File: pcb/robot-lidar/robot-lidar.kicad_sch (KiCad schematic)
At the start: 29 parts, among them J2 YLIDAR X4, J3 Jack-DC, J5 Conn_02x03_Odd_Even, J7 Conn_ARM_SWD_TagConnect_TC2030, U1 STM32F429VETx, U2 LM317-3.3_SOT-223, U2 MPU-6050, Y1 Crystal

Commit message: add rst
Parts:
- added R4: 10k, Resistor_SMD:R_0603_1608Metric, symbol Device:R_Small
- added SW1: SW_SPST, Button_Switch_SMD:SW_SPST_CK_RS282G05A3, symbol Switch:SW_SPST
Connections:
- net +3V3: now also R4.2
- net GND: now also SW1.1 (A)
- net RESET: now also U1.14 (NRST), R4.1, SW1.2 (B)
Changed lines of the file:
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@@
   (junction (at 237.49 97.79) (diameter 0) (color 0 0 0 0)
   )
+  (junction (at 52.07 49.53) (diameter 0) (color 0 0 0 0)
+  )
   (junction (at 85.09 21.59) (diameter 0) (color 0 0 0 0)
   )
@@
   (junction (at 242.57 59.69) (diameter 0) (color 0 0 0 0)
   )
+  (junction (at 48.26 49.53) (diameter 0) (color 0 0 0 0)
+  )
   (junction (at 236.22 -19.05) (diameter 0) (color 0 0 0 0)
   )
@@
     (stroke (width 0) (type default))
   )
+  (wire (pts (xy 52.07 49.53) (xy 54.61 49.53))
+    (stroke (width 0) (type default))
+  )
   (wire (pts (xy 87.63 21.59) (xy 87.63 41.91))
     (stroke (width 0) (type default))
   )
+  (wire (pts (xy 31.75 49.53) (xy 34.29 49.53))
+    (stroke (width 0) (type default))
+  )
   (wire (pts (xy 232.41 97.79) (xy 237.49 97.79))
     (stroke (width 0) (type default))
@@
     (stroke (width 0) (type default))
   )
+  (wire (pts (xy 48.26 49.53) (xy 52.07 49.53))
+    (stroke (width 0) (type default))
+  )
   (wire (pts (xy 229.87 -19.05) (xy 236.22 -19.05))
     (stroke (width 0) (type default))
@@
     (stroke (width 0) (type default))
   )
+  (wire (pts (xy 48.26 40.64) (xy 48.26 43.18))
+    (stroke (width 0) (type default))
+  )
   (wire (pts (xy 208.28 123.19) (xy 208.28 135.89))
     (stroke (width 0) (type default))
@@
     (stroke (width 0) (type default))
   )
+  (wire (pts (xy 48.26 49.53) (xy 48.26 48.26))
+    (stroke (width 0) (type default))
+  )
   (wire (pts (xy 261.62 59.69) (xy 270.51 59.69))
     (stroke (width 0) (type default))
@@
     (stroke (width 0) (type default))
   )
+  (wire (pts (xy 31.75 49.53) (xy 31.75 50.8))
+    (stroke (width 0) (type default))
+  )
   (wire (pts (xy 237.49 97.79) (xy 241.3 97.79))
     (stroke (width 0) (type default))
@@
     (stroke (width 0) (type default))
   )
+  (wire (pts (xy 44.45 49.53) (xy 48.26 49.53))
+    (stroke (width 0) (type default))
+  )
   (wire (pts (xy 77.47 184.15) (xy 77.47 190.5))
     (stroke (width 0) (type default))
@@
   )
   (wire (pts (xy 261.62 71.12) (xy 261.62 69.85))
+    (stroke (width 0) (type default))
+  )
+  (wire (pts (xy 52.07 48.26) (xy 52.07 49.53))
     (stroke (width 0) (type default))
   )
@@
     )
   )
+  (global_label "RESET" (shape input) (at 52.07 48.26 90) (fields_autoplaced)
+    (effects (font (size 1.27 1.27)) (justify left))
+    (property "Intersheetrefs" "${INTERSHEET_REFS}" (at 52.07 39.5297 90)
+      (effects (font (size 1.27 1.27)) (justify left) hide)
+    )
+  )
   (symbol (lib_id "Device:R_Small") (at 171.45 -16.51 270) (unit 1)
     (in_bom yes) (on_board yes) (dnp no)
@@
     )
   )
+  (symbol (lib_id "Switch:SW_SPST") (at 39.37 49.53 0) (unit 1)
+    (in_bom yes) (on_board yes) (dnp no) (fields_autoplaced)
+    (property "Reference" "SW1" (at 39.37 43.18 0)
+      (effects (font (size 1.27 1.27)))
+    )
+    (property "Value" "SW_SPST" (at 39.37 45.72 0)
+      (effects (font (size 1.27 1.27)))
+    )
+    (property "Footprint" "Button_Switch_SMD:SW_SPST_CK_RS282G05A3" (at 39.37 49.53 0)
+      (effects (font (size 1.27 1.27)) hide)
+    )
+    (property "Datasheet" "~" (at 39.37 49.53 0)
+      (effects (font (size 1.27 1.27)) hide)
+    )
+    (pin "1")
+    (pin "2")
+    (instances
+      (project "tablet"
+        (path "/868516f5-1ea3-47ae-b277-3f67998564bb"
+          (reference "SW1") (unit 1)
+        )
+      )
+      (project "robot-lidar"
+        (path "/cb10bbf7-c2c1-4a0d-8947-ad707931d83b"
+          (reference "SW1") (unit 1)
+        )
+      )
+    )
+  )
   (symbol (lib_id "Device:C") (at 270.51 128.27 0) (unit 1)
     (in_bom yes) (on_board yes) (dnp no) (fields_autoplaced)
@@
         (path "/cb10bbf7-c2c1-4a0d-8947-ad707931d83b"
           (reference "#PWR05") (unit 1)
+        )
+      )
+    )
+  )
+  (symbol (lib_id "Device:R_Small") (at 48.26 45.72 180) (unit 1)
+    (in_bom yes) (on_board yes) (dnp no)
+    (property "Reference" "R4" (at 44.45 41.91 90)
+      (effects (font (size 1.27 1.27)))
+    )
+    (property "Value" "10k" (at 46.99 41.91 90)
+      (effects (font (size 1.27 1.27)))
+    )
+    (property "Footprint" "Resistor_SMD:R_0603_1608Metric" (at 48.26 45.72 0)
+      (effects (font (size 1.27 1.27)) hide)
+    )
+    (property "Datasheet" "~" (at 48.26 45.72 0)
+      (effects (font (size 1.27 1.27)) hide)
+    )
+    (pin "1")
+    (pin "2")
+    (instances
+      (project "tablet"
+        (path "/868516f5-1ea3-47ae-b277-3f67998564bb"
+          (reference "R4") (unit 1)
+        )
+      )
+      (project "robot-lidar"
+        (path "/cb10bbf7-c2c1-4a0d-8947-ad707931d83b"
+          (reference "R7") (unit 1)
         )
       )
@@
     )
   )
+  (symbol (lib_id "power:+3V3") (at 48.26 40.64 0) (unit 1)
+    (in_bom yes) (on_board yes) (dnp no)
+    (property "Reference" "#PWR012" (at 48.26 44.45 0)
+      (effects (font (size 1.27 1.27)) hide)
+    )
+    (property "Value" "+3V3" (at 44.45 38.1 0)
+      (effects (font (size 1.27 1.27)))
+    )
+    (property "Footprint" "" (at 48.26 40.64 0)
+      (effects (font (size 1.27 1.27)) hide)
+    )
+    (property "Datasheet" "" (at 48.26 40.64 0)
+      (effects (font (size 1.27 1.27)) hide)
+    )
+    (pin "1")
+    (instances
+      (project "tablet"
+        (path "/868516f5-1ea3-47ae-b277-3f67998564bb"
+          (reference "#PWR012") (unit 1)
+        )
+      )
+      (project "robot-lidar"
+        (path "/cb10bbf7-c2c1-4a0d-8947-ad707931d83b"
+          (reference "#PWR021") (unit 1)
+        )
+      )
+    )
+  )
   (symbol (lib_id "power:+3V3") (at 115.57 -29.21 0) (unit 1)
     (in_bom yes) (on_board yes) (dnp no)
@@
         )
       )
+    )
+  )
+  (symbol (lib_id "power:GND") (at 31.75 50.8 0) (unit 1)
+    (in_bom yes) (on_board yes) (dnp no) (fields_autoplaced)
+    (property "Reference" "#PWR013" (at 31.75 57.15 0)
+      (effects (font (size 1.27 1.27)) hide)
+    )
+    (property "Value" "GND" (at 31.75 55.88 0)
+      (effects (font (size 1.27 1.27)))
+    )
+    (property "Footprint" "" (at 31.75 50.8 0)
+      (effects (font (size 1.27 1.27)) hide)
+    )
+    (property "Datasheet" "" (at 31.75 50.8 0)
+      (effects (font (size 1.27 1.27)) hide)
+    )
+    (pin "1")
+    (instances
+      (project "tablet"
+        (path "/868516f5-1ea3-47ae-b277-3f67998564bb"
+          (reference "#PWR013") (unit 1)
+        )
+      )
+      (project "robot-lidar"
+        (path "/cb10bbf7-c2c1-4a0d-8947-ad707931d83b"
+          (reference "#PWR020") (unit 1)
+        )
+      )

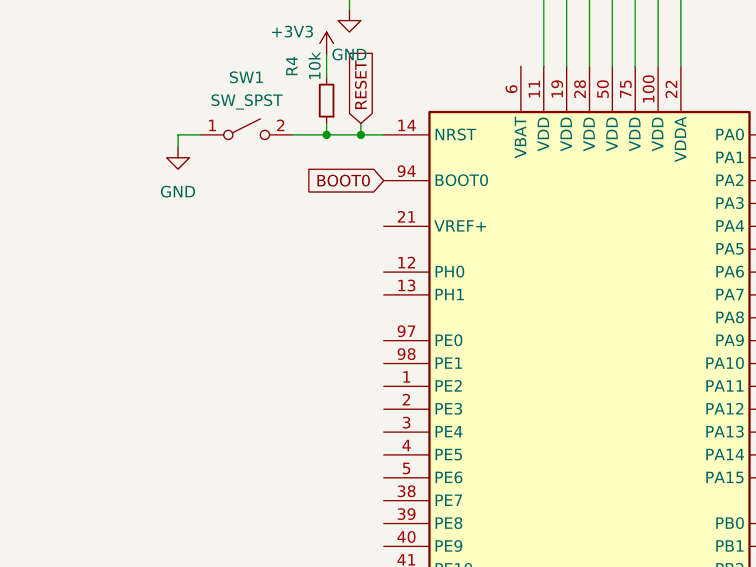
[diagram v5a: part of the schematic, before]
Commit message: wire crystal
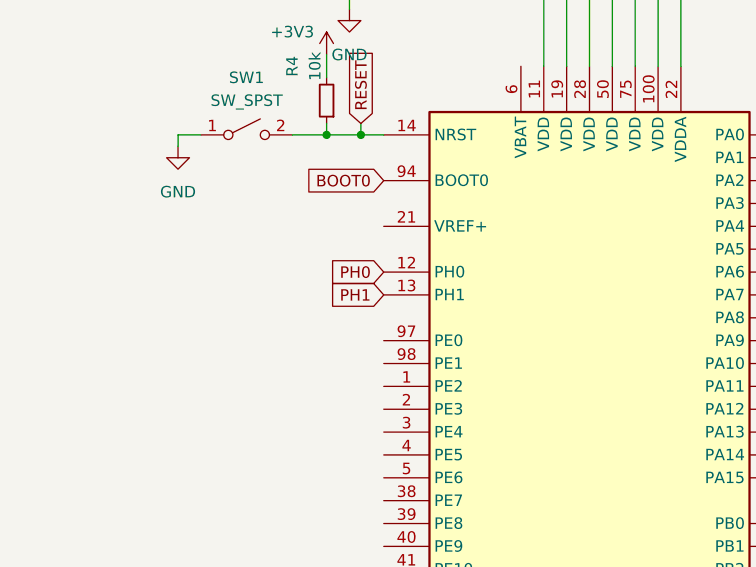
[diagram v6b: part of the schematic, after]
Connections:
- net PH0: now also U1.12 (PH0)
- net PH1: now also U1.13 (PH1)
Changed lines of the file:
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@@
+    )
+  )
+  (global_label "PH1" (shape input) (at 54.61 67.31 180) (fields_autoplaced)
+    (effects (font (size 1.27 1.27)) (justify right))
+    (property "Intersheetrefs" "${INTERSHEET_REFS}" (at 47.8148 67.31 0)
+      (effects (font (size 1.27 1.27)) (justify right) hide)
     )
   )
@@
     )
   )
+  (global_label "PH0" (shape input) (at 54.61 64.77 180) (fields_autoplaced)
+    (effects (font (size 1.27 1.27)) (justify right))
+    (property "Intersheetrefs" "${INTERSHEET_REFS}" (at 47.8148 64.77 0)
+      (effects (font (size 1.27 1.27)) (justify right) hide)
+    )
+  )

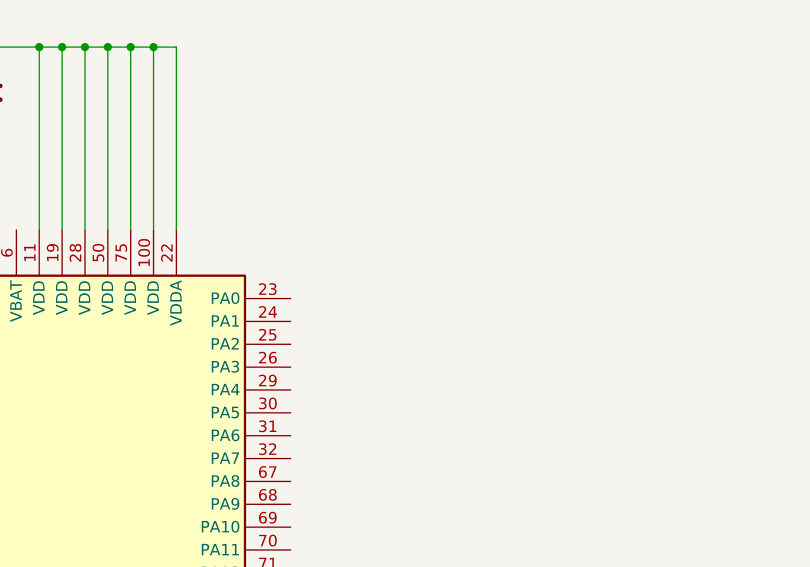
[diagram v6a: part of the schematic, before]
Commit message: add leds
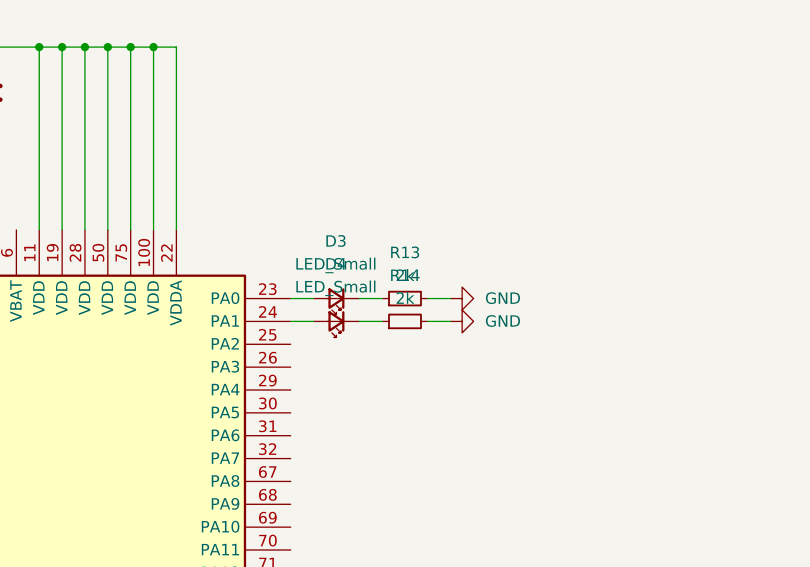
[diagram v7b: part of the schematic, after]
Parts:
- added D3, D4: LED_Small, Resistor_SMD:R_0603_1608Metric, symbol Device:LED_Small
- added R13, R14: 2k, Resistor_SMD:R_0603_1608Metric, symbol Device:R_Small
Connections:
- net GND: now also R13.2, R14.2
- net at U1.23 (PA0): now also D3.2 (A)
- net at U1.24 (PA1): now also D4.2 (A)
- new net: D4.1 (K), R14.1
- new net: D3.1 (K), R13.1
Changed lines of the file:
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@@
+    (stroke (width 0) (type default))
+  )
+  (wire (pts (xy 107.95 49.53) (xy 110.49 49.53))
     (stroke (width 0) (type default))
   )
@@
     (stroke (width 0) (type default))
   )
+  (wire (pts (xy 100.33 52.07) (xy 102.87 52.07))
+    (stroke (width 0) (type default))
+  )
+  (wire (pts (xy 115.57 49.53) (xy 118.11 49.53))
+    (stroke (width 0) (type default))
+  )
   (wire (pts (xy 251.46 71.12) (xy 251.46 73.66))
     (stroke (width 0) (type default))
@@
     (stroke (width 0) (type default))
   )
+  (wire (pts (xy 115.57 52.07) (xy 118.11 52.07))
+    (stroke (width 0) (type default))
+  )
   (wire (pts (xy 224.79 -13.97) (xy 224.79 -19.05))
     (stroke (width 0) (type default))
@@
     (stroke (width 0) (type default))
   )
+  (wire (pts (xy 102.87 49.53) (xy 100.33 49.53))
+    (stroke (width 0) (type default))
+  )
   (wire (pts (xy 270.51 132.08) (xy 270.51 135.89))
     (stroke (width 0) (type default))
@@
   )
   (wire (pts (xy 20.32 21.59) (xy 27.94 21.59))
+    (stroke (width 0) (type default))
+  )
+  (wire (pts (xy 107.95 52.07) (xy 110.49 52.07))
     (stroke (width 0) (type default))
   )
@@
     )
   )
+  (symbol (lib_id "Device:LED_Small") (at 105.41 52.07 180) (unit 1)
+    (in_bom yes) (on_board yes) (dnp no) (fields_autoplaced)
+    (property "Reference" "D4" (at 105.3465 45.72 0)
+      (effects (font (size 1.27 1.27)))
+    )
+    (property "Value" "LED_Small" (at 105.3465 48.26 0)
+      (effects (font (size 1.27 1.27)))
+    )
+    (property "Footprint" "Resistor_SMD:R_0603_1608Metric" (at 105.41 52.07 90)
+      (effects (font (size 1.27 1.27)) hide)
+    )
+    (property "Datasheet" "~" (at 105.41 52.07 90)
+      (effects (font (size 1.27 1.27)) hide)
+    )
+    (pin "1")
+    (pin "2")
+    (instances
+      (project "tablet"
+        (path "/868516f5-1ea3-47ae-b277-3f67998564bb"
+          (reference "D4") (unit 1)
+        )
+      )
+      (project "robot-lidar"
+        (path "/cb10bbf7-c2c1-4a0d-8947-ad707931d83b"
+          (reference "D2") (unit 1)
+        )
+      )
+    )
+  )
   (symbol (lib_id "Device:R_Small") (at 171.45 -16.51 270) (unit 1)
     (in_bom yes) (on_board yes) (dnp no)
@@
     )
   )
+  (symbol (lib_id "power:GND") (at 118.11 52.07 90) (unit 1)
+    (in_bom yes) (on_board yes) (dnp no) (fields_autoplaced)
+    (property "Reference" "#PWR032" (at 124.46 52.07 0)
+      (effects (font (size 1.27 1.27)) hide)
+    )
+    (property "Value" "GND" (at 121.92 52.07 90)
+      (effects (font (size 1.27 1.27)) (justify right))
+    )
+    (property "Footprint" "" (at 118.11 52.07 0)
+      (effects (font (size 1.27 1.27)) hide)
+    )
+    (property "Datasheet" "" (at 118.11 52.07 0)
+      (effects (font (size 1.27 1.27)) hide)
+    )
+    (pin "1")
+    (instances
+      (project "tablet"
+        (path "/868516f5-1ea3-47ae-b277-3f67998564bb"
+          (reference "#PWR032") (unit 1)
+        )
+      )
+      (project "robot-lidar"
+        (path "/cb10bbf7-c2c1-4a0d-8947-ad707931d83b"
+          (reference "#PWR023") (unit 1)
+        )
+      )
+    )
+  )
   (symbol (lib_id "Regulator_Linear:LM317_SOT-223") (at 251.46 59.69 0) (unit 1)
     (in_bom yes) (on_board yes) (dnp no) (fields_autoplaced)
@@
         (path "/cb10bbf7-c2c1-4a0d-8947-ad707931d83b"
           (reference "SW1") (unit 1)
+        )
+      )
+    )
+  )
+  (symbol (lib_id "Device:R_Small") (at 113.03 49.53 90) (unit 1)
+    (in_bom yes) (on_board yes) (dnp no) (fields_autoplaced)
+    (property "Reference" "R13" (at 113.03 44.45 90)
+      (effects (font (size 1.27 1.27)))
+    )
+    (property "Value" "2k" (at 113.03 46.99 90)
+      (effects (font (size 1.27 1.27)))
+    )
+    (property "Footprint" "Resistor_SMD:R_0603_1608Metric" (at 113.03 49.53 0)
+      (effects (font (size 1.27 1.27)) hide)
+    )
+    (property "Datasheet" "~" (at 113.03 49.53 0)
+      (effects (font (size 1.27 1.27)) hide)
+    )
+    (pin "1")
+    (pin "2")
+    (instances
+      (project "tablet"
+        (path "/868516f5-1ea3-47ae-b277-3f67998564bb"
+          (reference "R13") (unit 1)
+        )
+      )
+      (project "drone"
+        (path "/8d172cff-266e-4e68-aa3f-17546d01ba91"
+          (reference "R11") (unit 1)
+        )
+      )
+      (project "robot-lidar"
+        (path "/cb10bbf7-c2c1-4a0d-8947-ad707931d83b"
+          (reference "R8") (unit 1)
         )
       )
@@
     )
   )
+  (symbol (lib_id "Device:R_Small") (at 113.03 52.07 90) (unit 1)
+    (in_bom yes) (on_board yes) (dnp no) (fields_autoplaced)
+    (property "Reference" "R14" (at 113.03 46.99 90)
+      (effects (font (size 1.27 1.27)))
+    )
+    (property "Value" "2k" (at 113.03 49.53 90)
+      (effects (font (size 1.27 1.27)))
+    )
+    (property "Footprint" "Resistor_SMD:R_0603_1608Metric" (at 113.03 52.07 0)
+      (effects (font (size 1.27 1.27)) hide)
+    )
+    (property "Datasheet" "~" (at 113.03 52.07 0)
+      (effects (font (size 1.27 1.27)) hide)
+    )
+    (pin "1")
+    (pin "2")
+    (instances
+      (project "tablet"
+        (path "/868516f5-1ea3-47ae-b277-3f67998564bb"
+          (reference "R14") (unit 1)
+        )
+      )
+      (project "drone"
+        (path "/8d172cff-266e-4e68-aa3f-17546d01ba91"
+          (reference "R11") (unit 1)
+        )
+      )
+      (project "robot-lidar"
+        (path "/cb10bbf7-c2c1-4a0d-8947-ad707931d83b"
+          (reference "R9") (unit 1)
+        )
+      )
+    )
+  )
   (symbol (lib_id "power:+3V3") (at 115.57 -29.21 0) (unit 1)
     (in_bom yes) (on_board yes) (dnp no)
@@
         (path "/cb10bbf7-c2c1-4a0d-8947-ad707931d83b"
           (reference "#PWR017") (unit 1)
+        )
+      )
+    )
+  )
+  (symbol (lib_id "Device:LED_Small") (at 105.41 49.53 180) (unit 1)
+    (in_bom yes) (on_board yes) (dnp no) (fields_autoplaced)
+    (property "Reference" "D3" (at 105.3465 43.18 0)
+      (effects (font (size 1.27 1.27)))
+    )
+    (property "Value" "LED_Small" (at 105.3465 45.72 0)
+      (effects (font (size 1.27 1.27)))
+    )
+    (property "Footprint" "Resistor_SMD:R_0603_1608Metric" (at 105.41 49.53 90)
+      (effects (font (size 1.27 1.27)) hide)
+    )
+    (property "Datasheet" "~" (at 105.41 49.53 90)
+      (effects (font (size 1.27 1.27)) hide)
+    )
+    (pin "1")
+    (pin "2")
+    (instances
+      (project "tablet"
+        (path "/868516f5-1ea3-47ae-b277-3f67998564bb"
+          (reference "D3") (unit 1)
+        )
+      )
+      (project "robot-lidar"
+        (path "/cb10bbf7-c2c1-4a0d-8947-ad707931d83b"
+          (reference "D1") (unit 1)
         )
       )
@@
         )
       )
+    )
+  )
+  (symbol (lib_id "power:GND") (at 118.11 49.53 90) (unit 1)
+    (in_bom yes) (on_board yes) (dnp no) (fields_autoplaced)
+    (property "Reference" "#PWR031" (at 124.46 49.53 0)
+      (effects (font (size 1.27 1.27)) hide)
+    )
+    (property "Value" "GND" (at 121.92 49.53 90)
+      (effects (font (size 1.27 1.27)) (justify right))
+    )
+    (property "Footprint" "" (at 118.11 49.53 0)
+      (effects (font (size 1.27 1.27)) hide)
+    )
+    (property "Datasheet" "" (at 118.11 49.53 0)
+      (effects (font (size 1.27 1.27)) hide)
+    )
+    (pin "1")
+    (instances
+      (project "tablet"
+        (path "/868516f5-1ea3-47ae-b277-3f67998564bb"
+          (reference "#PWR031") (unit 1)
+        )
+      )
+      (project "robot-lidar"
+        (path "/cb10bbf7-c2c1-4a0d-8947-ad707931d83b"
+          (reference "#PWR022") (unit 1)
+        )
+      )

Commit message: add wiring motor
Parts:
- added U4, U5: MX1508, MX1508:SOIC127P600X177-16N, symbol MX1508:MX1508
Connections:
- net MOTOR_4_B: now reaches U1.67 (PA8)
- net MOTOR_4_B: now also U5.7 (INB2)
- net MOTOR_4_A: now reaches U1.68 (PA9)
- net MOTOR_4_A: now also U5.6 (INA2)
- net MOTOR_3_B: now reaches U1.69 (PA10)
- net MOTOR_3_B: now also U5.3 (INB1)
- net MOTOR_3_A: now reaches U1.70 (PA11)
- net MOTOR_3_A: now also U5.2 (INA1)
- net MOTOR_2_B: now reaches U1.71 (PA12)
- net MOTOR_2_B: now also U4.7 (INB2)
- net MOTOR_2_A: now reaches U1.72 (PA13)
- net MOTOR_2_A: now also U4.6 (INA2)
- net MOTOR_1_B: now reaches U1.76 (PA14)
- net MOTOR_1_B: now also U4.3 (INB1)
- net MOTOR_1_A: now reaches U1.77 (PA15)
- net MOTOR_1_A: now also U4.2 (INA1)
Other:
- moved on the sheet: C1, C14, C15, C2, C3, J2, J3, J5, J7, R1, R2, R6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
